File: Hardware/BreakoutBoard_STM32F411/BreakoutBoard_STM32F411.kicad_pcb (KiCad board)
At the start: 4 copper layers, 21.4 x 50.2 mm, 42 parts, among them IC101 STM32F411CCU6TR, IC401 TLV77333PDBVR, IC402 TLV77333PDBVR, J201 GSB1C41110SSHR, J202 PortB1, J203 PortB2, J204 PortA1, J205 PortA2, J403 Conn_02x03_Odd_Even, J404 SYS_JTAG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

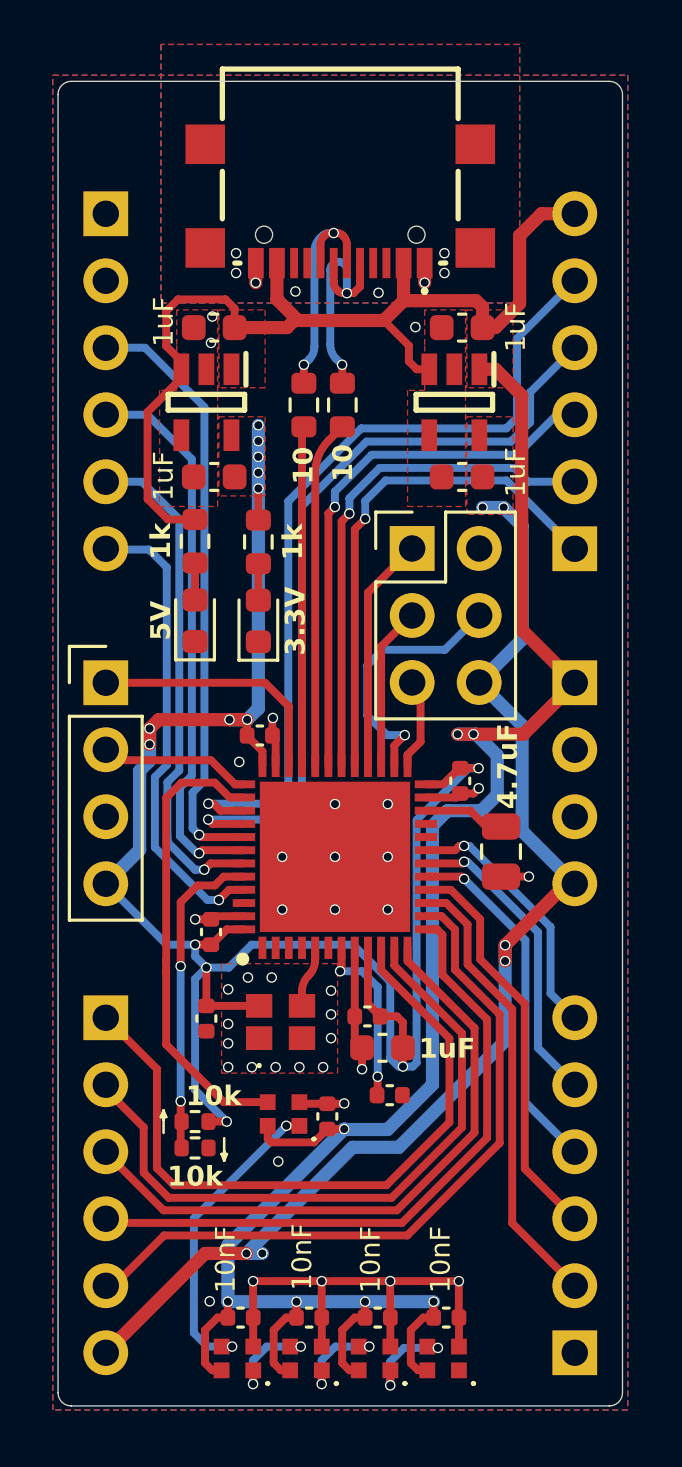
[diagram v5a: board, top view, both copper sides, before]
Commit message: added:labeling, changed:5V to 3V3P
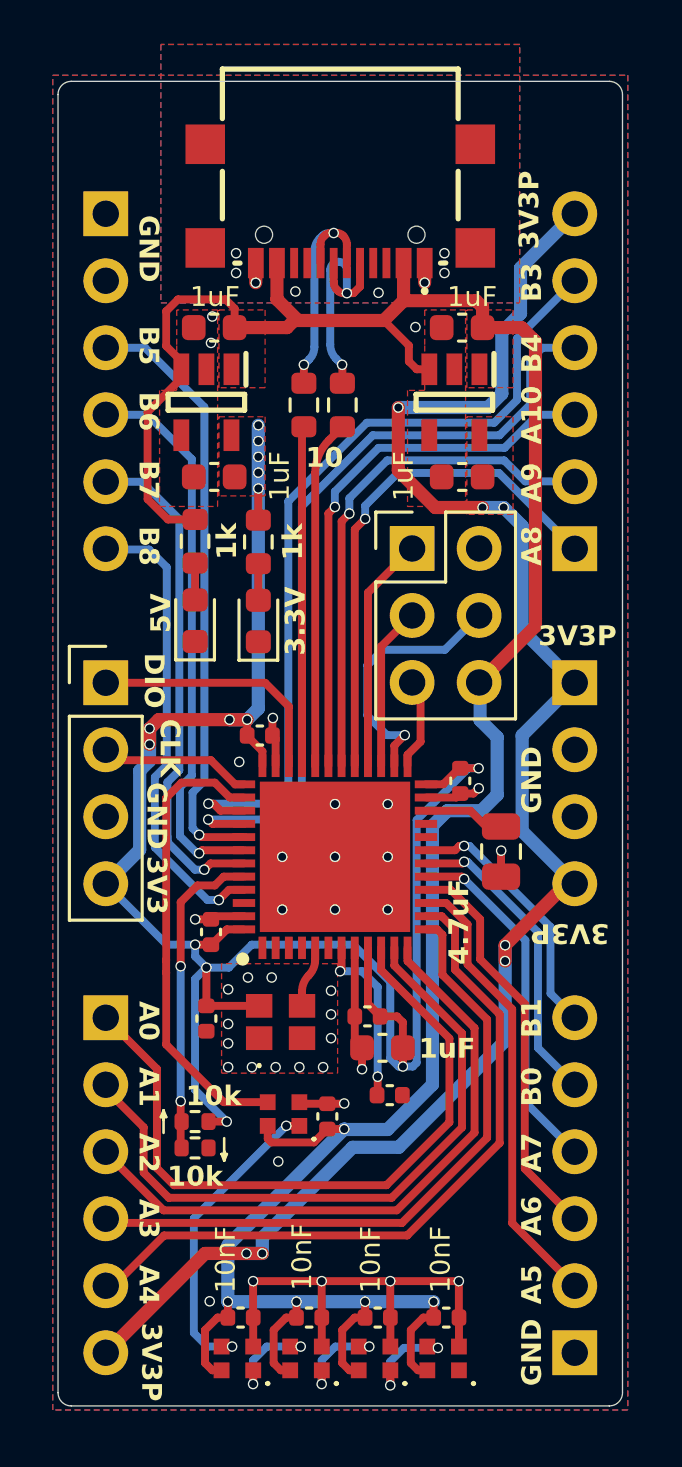
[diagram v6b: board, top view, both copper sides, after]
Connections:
- J204 pad 6: +5V -> +3.3VP
- J403 pad 6: +3.3VP -> +5V
- J405 pad 1: +5V -> +3.3VP
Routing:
- net +3.3VP: track 45.7 -> 65.3 mm, vias 6 -> 7
- net +5V: track 110.8 -> 102.3 mm, vias 7 -> 5
- net PA10: track 20.1 -> 20.8 mm
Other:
- board text added: "3V3"
- board text added: "3V3P"
- board text added: "A0"
- board text added: "A1"
- board text added: "A10"
- board text added: "A2"
- board text added: "A3"
- board text added: "A4"
- board text added: "A5"
- board text added: "A6"
- board text added: "A7"
- board text added: "A8"
- board text added: "A9"
- board text added: "B0"
- board text added: "B1"
- board text added: "B3"
- board text added: "B4"
- board text added: "B5"
- board text added: "B6"
- board text added: "B7"
- board text added: "B8"
- board text added: "CLK"
- board text added: "DIO"
- board text added: "GND"

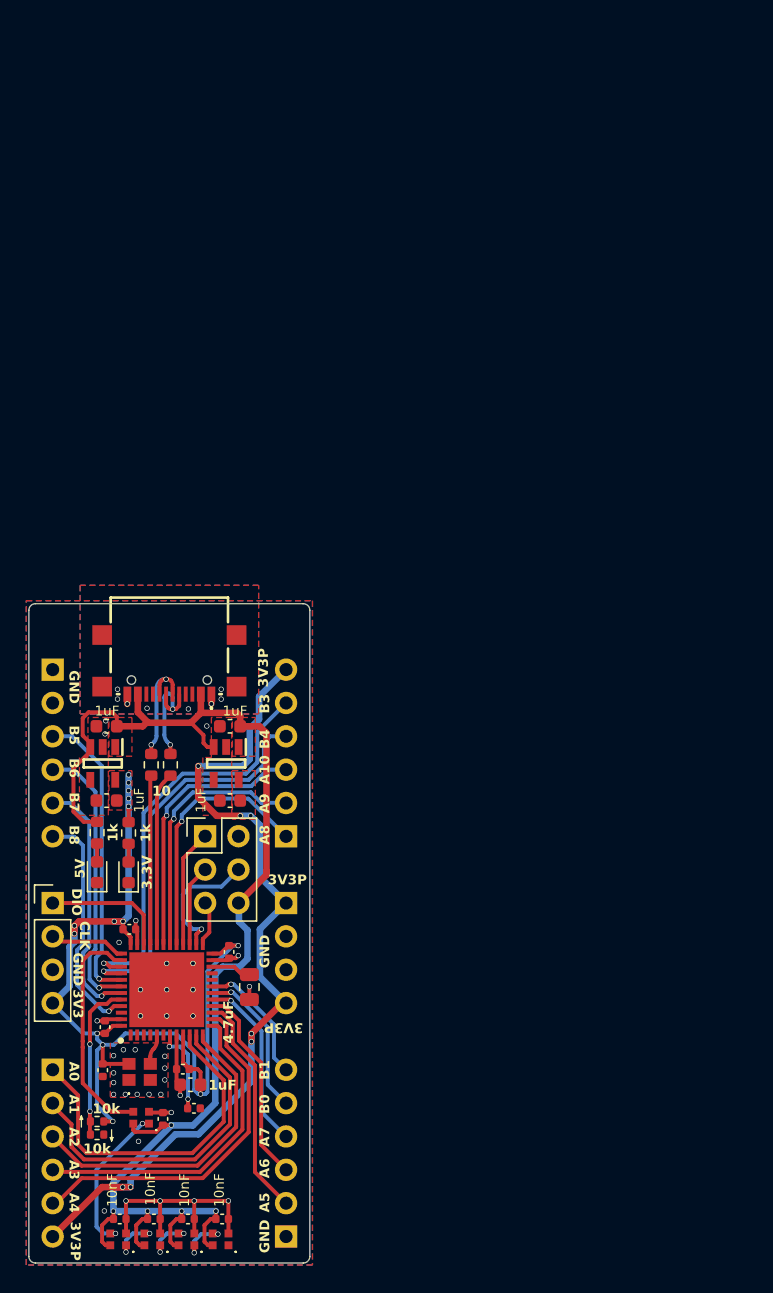
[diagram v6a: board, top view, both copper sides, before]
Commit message: fixed:edgecut, checked:pinheader spacing
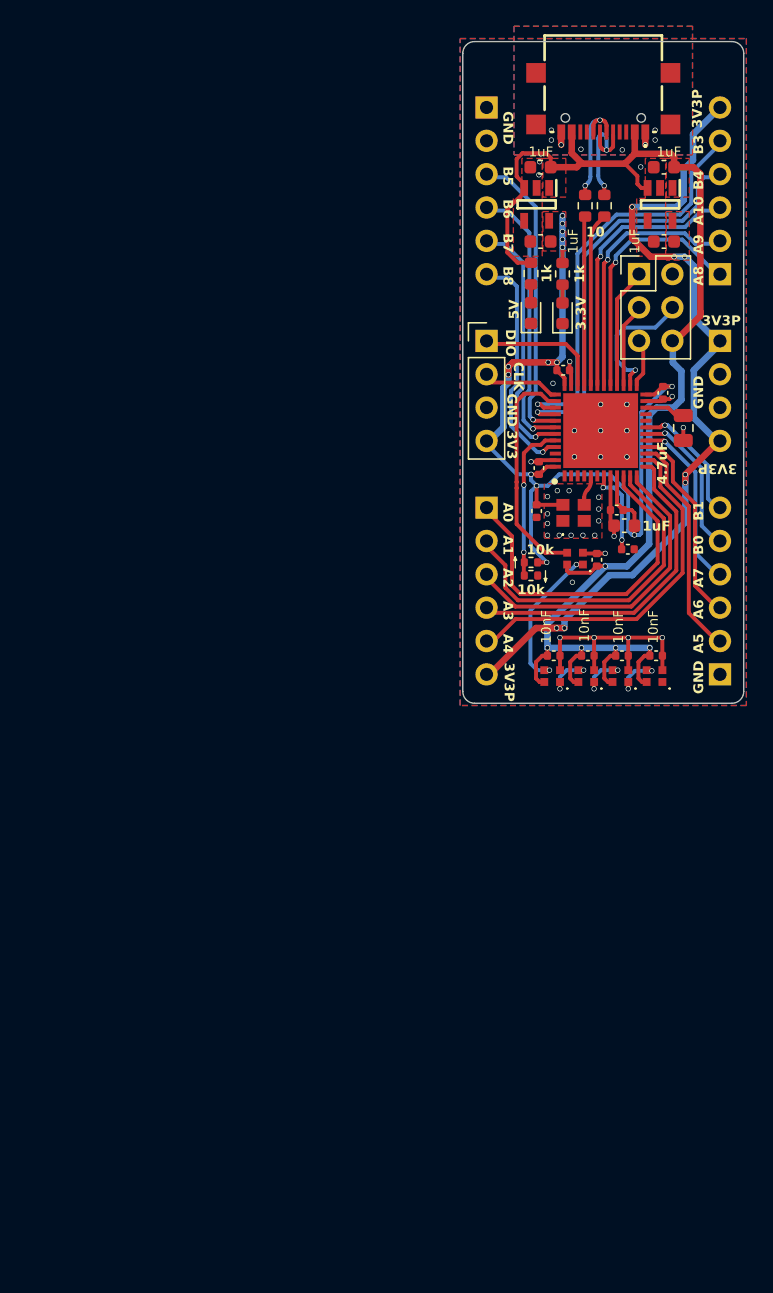
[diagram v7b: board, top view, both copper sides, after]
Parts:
- moved LED601 54.2 mm to (190.6, 108.6)
- moved LED701 54.2 mm to (193.2, 108.6)
- moved LED801 54.2 mm to (195.8, 108.6)
- moved C601 54.2 mm to (190.7, 107.1)
- moved C701 54.2 mm to (193.3, 107.1)
- moved C801 54.2 mm to (195.9, 107.1)
- moved C901 54.2 mm to (198.5, 107.1)
- moved LED901 54.2 mm to (198.4, 108.6)
- moved J203 54.1 mm to (203.3, 108.5)
- moved J204 54.1 mm to (203.3, 78.0)
- moved J205 54.1 mm to (185.6, 65.3)
- moved J403 54.1 mm to (197.2, 78.0)
- moved J404 54.1 mm to (185.6, 83.1)
- moved J405 54.1 mm to (203.3, 83.1)
- moved J201 54.1 mm to (194.4, 63.8)
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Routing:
- net GND: vias 45 -> 44
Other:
- board size 21.4 x 50.2 mm -> 21.4 x 50.4 mm

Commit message: ordering Version
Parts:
- C103: value 100nF -> 10nF
- moved J403 0.23 mm to (197.2, 78.3)
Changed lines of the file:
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@@
 		(attr through_hole)
 		(fp_line
-			(start 4.47 3.965)
-			(end 4.47 2.088)
-			(stroke
-				(width 0.2)
-				(type solid)
-			)
-			(layer "F.SilkS")
-		)
-		(fp_line
 			(start 4.47 0.088)
 			(end 4.47 -1.712)
@@
 		)
 		(fp_line
-			(start -4.47 3.965)
-			(end 4.47 3.965)
-			(stroke
-				(width 0.2)
-				(type solid)
-			)
-			(layer "F.SilkS")
-		)
-		(fp_line
-			(start -4.47 2.088)
-			(end -4.47 3.965)
-			(stroke
-				(width 0.2)
-				(type solid)
-			)
-			(layer "F.SilkS")
-		)
-		(fp_line
 			(start -4.47 -1.712)
 			(end -4.47 0.088)
@@
 	(footprint "Connector_PinHeader_2.54mm:PinHeader_2x03_P2.54mm_Vertical"
 		(layer "F.Cu")
-		(at 197.175 78.026)
+		(at 197.175 78.26)
 		(descr "Through hole straight pin header, 2x03, 2.54mm pitch, double rows")
 		(tags "Through hole pin header THT 2x03 2.54mm double row")
@@
 			)
 		)
-		(property "Value" "100nF"
-			(at 0 -1 90)
+		(property "Value" "10nF"
+			(at 0 -0.874 90)
 			(layer "F.SilkS")
-			(hide yes)
 			(effects
 				(font
@@
 	)
 	(gr_text "3V3P"
-		(at 186.85 107.616 270)
+		(at 186.8 107.2 270)
 		(layer "F.SilkS")
 		(effects
@@
 	)
 	(segment
-		(start 188.4 100.951)
-		(end 188.435 100.986)
-		(width 0.3)
-		(layer "F.Cu")
-		(net 6)
-	)
-	(segment
 		(start 189.695 91.035)
 		(end 190.03 90.7)
@@
 	(segment
 		(start 201.85 70.416)
-		(end 201.85 80.916)
+		(end 201.85 81.205)
 		(width 0.5)
 		(layer "F.Cu")
@@
 	(segment
 		(start 201.32 69.886)
-		(end 201.75 70.316)
+		(end 201.85 70.416)
 		(width 0.5)
 		(layer "F.Cu")
@@
 	)
 	(segment
-		(start 201.75 70.316)
-		(end 201.85 70.416)
-		(width 0.5)
-		(layer "F.Cu")
-		(net 12)
-	)
-	(segment
-		(start 201.85 80.916)
-		(end 201.85 81.205)
-		(width 0.5)
-		(layer "F.Cu")
-		(net 12)
-	)
-	(segment
 		(start 192.05 67.44)
 		(end 192.05 68.816)
@@
 	)
 	(segment
-		(start 199.75 83.375)
-		(end 199.715 83.34)
-		(width 0.5)
-		(layer "B.Cu")
-		(net 12)
-	)
-	(segment
 		(start 194.616 100.286)
 		(end 196.245 100.286)
@@
 	)
 	(segment
-		(start 193.7 66.726776)
-		(end 193.7 67.44)
-		(width 0.3)
-		(layer "F.Cu")
-		(net 16)
-	)
-	(segment
-		(start 194.538388 66.388388)
-		(end 194.575 66.425)
-		(width 0.3)
-		(layer "F.Cu")
-		(net 16)
-	)
-	(segment
-		(start 194.7 66.726776)
-		(end 194.7 67.44)
+		(start 193.7 66.490927)
+		(end 193.7 67.206)
 		(width 0.3)
 		(layer "F.Cu")
@@
 	)
 	(segment
-		(start 194.2 66.3)
-		(end 194.325 66.3)
+		(start 194.7 66.441421)
+		(end 194.7 67.206)
 		(width 0.3)
 		(layer "F.Cu")
@@
 	)
 	(segment
-		(start 193.861611 66.388388)
-		(end 193.825 66.425)
+		(start 193.833187 66.195812)
+		(end 193.8145 66.2145)
 		(width 0.3)
 		(layer "F.Cu")
@@
 	)
 	(segment
-		(start 194.075 66.3)
-		(end 194.2 66.3)
+		(start 194.0645 66.1)
+		(end 194.358578 66.1)
 		(width 0.3)
 		(layer "F.Cu")
@@
 	)
 	(via
-		(at 194.2 66.3)
+		(at 194.2 66.1)
 		(size 0.4)
 		(drill 0.3)
@@
 	)
 	(arc
-		(start 194.075 66.3)
-		(mid 193.959514 66.322971)
-		(end 193.861611 66.388388)
+		(start 193.8145 66.2145)
+		(mid 193.729757 66.341325)
+		(end 193.7 66.490927)
 		(width 0.3)
 		(layer "F.Cu")
@@
 	)
 	(arc
-		(start 194.575 66.425)
-		(mid 194.667513 66.563456)
-		(end 194.7 66.726776)
+		(start 194.0645 66.1)
+		(mid 193.939314 66.1249)
+		(end 193.833187 66.195812)
 		(width 0.3)
 		(layer "F.Cu")
@@
 	)
 	(arc
-		(start 194.538388 66.388388)
-		(mid 194.440484 66.322971)
-		(end 194.325 66.3)
+		(start 194.6 66.2)
+		(mid 194.67401 66.310764)
+		(end 194.7 66.441421)
 		(width 0.3)
 		(layer "F.Cu")
@@
 	)
 	(arc
-		(start 193.825 66.425)
-		(mid 193.732486 66.563456)
-		(end 193.7 66.726776)
+		(start 194.6 66.2)
+		(mid 194.489234 66.125989)
+		(end 194.358578 66.1)
 		(width 0.3)
 		(layer "F.Cu")
@@
 	)
 	(segment
-		(start 194.2 66.3)
-		(end 194.0375 66.3)
-		(width 0.3)
-		(layer "B.Cu")
-		(net 16)
-	)
-	(segment
-		(start 193.27 71.095)
-		(end 193.07 71.295)
+		(start 193.47 67.346187)
+		(end 193.47 70.612157)
 		(width 0.3)
 		(layer "B.Cu")
@@
 	)
 	(segment
-		(start 193.672499 66.502499)
-		(end 193.760095 66.414904)
+		(start 193.07 71.295)
+		(end 193.27 71.095)
 		(width 0.3)
 		(layer "B.Cu")
@@
 	)
 	(segment
-		(start 193.47 70.612157)
-		(end 193.47 66.991378)
+		(start 193.835 66.465)
+		(end 194.2 66.1)
 		(width 0.3)
 		(layer "B.Cu")
@@
 	)
 	(arc
-		(start 193.47 70.612157)
+		(start 193.27 71.095)
 		(mid 193.418021 70.873469)
-		(end 193.27 71.095)
-		(width 0.3)
-		(layer "B.Cu")
-		(net 16)
-	)
-	(arc
-		(start 194.0375 66.3)
-		(mid 193.887369 66.329862)
-		(end 193.760095 66.414904)
+		(end 193.47 70.612157)
 		(width 0.3)
 		(layer "B.Cu")
@@
 	)
 	(arc
-		(start 193.672499 66.502499)
-		(mid 193.522627 66.726798)
-		(end 193.47 66.991378)
+		(start 193.835 66.465)
+		(mid 193.56486 66.869292)
+		(end 193.47 67.346187)
 		(width 0.3)
 		(layer "B.Cu")
@@
 	)
 	(segment
-		(start 194.919 100.962)
-		(end 192.2575 103.6235)
-		(width 0.5)
-		(layer "B.Cu")
-		(net 27)
-	)
-	(segment
 		(start 200.645 76.706)
 		(end 201.345 77.406)
@@
 	)
 	(segment
-		(start 192.2575 103.6235)
-		(end 191.495003 104.385997)
+		(start 191.495003 104.385997)
+		(end 194.919 100.962)
 		(width 0.5)
 		(layer "B.Cu")
@@
 	)
 	(segment
-		(start 187.897 89.392232)
-		(end 187.897 89.166)
-		(width 0.3)
-		(layer "B.Cu")
-		(net 30)
-	)
-	(segment
 		(start 186.93 75.73)
 		(end 185.56 75.73)
@@
 	)
 	(segment
-		(start 203.326 75.716)
-		(end 203.34 75.73)
-		(width 0.3)
-		(layer "B.Cu")
-		(net 31)
-	)
-	(segment
 		(start 194.795 76.936)
 		(end 194.795 76.355)
@@
 			"9061a6f7-eedd-483a-aec2-3530d2bac3f8" "90b166ae-a0ea-4d6e-8b0b-4fde08300241"
 			"936b8314-0eb6-4224-8117-2000cd565a02" "97bbe1d8-72db-4914-9a70-fd7c72119746"
-			"984f31a5-17ad-4061-8313-116940e000dd" "991fb4ac-1f2a-4d77-8cf2-79be67d57af3"
-			"9cb01bc6-f38f-4fba-b2ba-33f76ca87221" "9cd24a0e-a724-4348-b8ad-484d0c1a3001"
-			"9d644d6d-1e8b-423e-a5e4-a25d8ca834ef" "9d738cbf-352f-40ce-b5aa-fa63ccd88a1a"
-			"9e18b3f2-1e46-49a2-a706-e4cac73ffcb8" "a1d5b478-9ac3-4b28-8aae-2988abdd0572"
-			"a351a675-6d8b-4ff2-8748-2cb112c3b405" "a53f6680-eaba-4985-ac9e-ed84e3df646a"
-			"a555c708-b102-4f1a-be2a-a689c23cd8ec" "ab333ac0-a337-41c5-9150-578df3b367e6"
-			"b1eab8bd-b6ba-492d-aac5-a8e8896055d8" "b2217b2a-8e00-4a06-b598-266261e4eca8"
-			"b26543e5-96d5-4b91-8413-00303e6b4274" "b3a3bb48-13a9-400a-a722-dbda411d75c0"
-			"b458ac56-e53f-4d13-84c4-92fb74e09e12" "b4da50cf-0282-4bf5-923d-be5a7b8191e0"
-			"b602e55f-b784-4f36-a5f3-84856b895711" "bfcf2464-90be-4c06-9f70-c4a3a912ad30"
-			"bfebfd38-61cd-4705-960c-bdce302ebfb5" "c57a648f-f596-4ca3-b35d-0cd6752680e2"
-			"c664858a-f964-497c-8b71-8a1ccb30c498" "c72a436c-2bdd-42ce-91d9-954576c4727f"
-			"c8b13321-2ba2-41bf-a993-9f90bcd615a5" "c8f8d109-0595-41b5-bcce-7cb4bd7cf8e0"
-			"cac0fa3d-05a8-4515-90c7-5fe0d7916d1d" "cd0c786f-1a32-4fc4-8c24-38417479ae6b"
-			"d0a241f3-d2bd-4745-8e01-00debd98c49c" "d143fa5b-8cab-4841-9d66-2129df6020aa"
-			"d763e94b-b635-4bec-9953-ca6525b68e35" "dac34644-a048-4e1b-b88a-4f5232ee763c"
-			"dc3b8b37-aac5-49f6-b07b-07e300ca9e31" "dfb37506-ca03-4e47-8074-ac52613f0644"
-			"dfec2621-b790-4109-92d0-f6b09e22c382" "e12d0c51-8cfb-4a45-9466-9ca911815a68"
-			"e304ad46-f9f9-42dc-bc7b-086198585db6" "e42ec4d1-e99e-44af-b534-4d5318db9cfa"
-			"e4bfd52b-f2a3-42d7-8cdf-fcb16f10c8f5" "e554f08f-1b4f-4c6f-82fa-140e659def1f"
-			"e5761d27-32e3-4733-b706-b9df3f760663" "e7dbbc27-b770-434d-b0ba-3e0cd8fb83c5"
-			"ea481244-7b68-44be-9d90-44ff0322417b" "ec2de171-9bc3-40fb-83bd-fa82f9cdc5f6"
-			"ec93b996-df20-4e16-94bc-281965e20196" "ee8a0531-57a4-41d8-8d52-f9ba57b33260"
-			"f310699c-b07c-4404-81c6-a341fc22b8b7" "f9fdce73-7e40-4588-8f04-669e471fcb59"
-			"fa182eb2-8ef1-4d65-95db-af8f546a3777" "fb4dcbba-132f-442f-8eb4-98ca91fb56aa"
+			"984f31a5-17ad-4061-8313-116940e000dd" "9cb01bc6-f38f-4fba-b2ba-33f76ca87221"
+			"9cd24a0e-a724-4348-b8ad-484d0c1a3001" "9d644d6d-1e8b-423e-a5e4-a25d8ca834ef"
+			"9d738cbf-352f-40ce-b5aa-fa63ccd88a1a" "9e18b3f2-1e46-49a2-a706-e4cac73ffcb8"
+			"a1d5b478-9ac3-4b28-8aae-2988abdd0572" "a351a675-6d8b-4ff2-8748-2cb112c3b405"
+			"a53f6680-eaba-4985-ac9e-ed84e3df646a" "a555c708-b102-4f1a-be2a-a689c23cd8ec"
+			"ab333ac0-a337-41c5-9150-578df3b367e6" "b1eab8bd-b6ba-492d-aac5-a8e8896055d8"
+			"b2217b2a-8e00-4a06-b598-266261e4eca8" "b26543e5-96d5-4b91-8413-00303e6b4274"
+			"b3a3bb48-13a9-400a-a722-dbda411d75c0" "b458ac56-e53f-4d13-84c4-92fb74e09e12"
+			"b4da50cf-0282-4bf5-923d-be5a7b8191e0" "b602e55f-b784-4f36-a5f3-84856b895711"
+			"bfcf2464-90be-4c06-9f70-c4a3a912ad30" "bfebfd38-61cd-4705-960c-bdce302ebfb5"
+			"c57a648f-f596-4ca3-b35d-0cd6752680e2" "c664858a-f964-497c-8b71-8a1ccb30c498"
+			"c72a436c-2bdd-42ce-91d9-954576c4727f" "c8b13321-2ba2-41bf-a993-9f90bcd615a5"
+			"c8f8d109-0595-41b5-bcce-7cb4bd7cf8e0" "cac0fa3d-05a8-4515-90c7-5fe0d7916d1d"
+			"cd0c786f-1a32-4fc4-8c24-38417479ae6b" "d0a241f3-d2bd-4745-8e01-00debd98c49c"
+			"d143fa5b-8cab-4841-9d66-2129df6020aa" "d763e94b-b635-4bec-9953-ca6525b68e35"
+			"dac34644-a048-4e1b-b88a-4f5232ee763c" "dc3b8b37-aac5-49f6-b07b-07e300ca9e31"
+			"dfb37506-ca03-4e47-8074-ac52613f0644" "dfec2621-b790-4109-92d0-f6b09e22c382"
+			"e12d0c51-8cfb-4a45-9466-9ca911815a68" "e304ad46-f9f9-42dc-bc7b-086198585db6"
+			"e42ec4d1-e99e-44af-b534-4d5318db9cfa" "e4bfd52b-f2a3-42d7-8cdf-fcb16f10c8f5"
+			"e554f08f-1b4f-4c6f-82fa-140e659def1f" "e5761d27-32e3-4733-b706-b9df3f760663"
+			"e7dbbc27-b770-434d-b0ba-3e0cd8fb83c5" "ea481244-7b68-44be-9d90-44ff0322417b"
+			"ec2de171-9bc3-40fb-83bd-fa82f9cdc5f6" "ec93b996-df20-4e16-94bc-281965e20196"
+			"ee8a0531-57a4-41d8-8d52-f9ba57b33260" "f310699c-b07c-4404-81c6-a341fc22b8b7"
+			"f9fdce73-7e40-4588-8f04-669e471fcb59" "fa182eb2-8ef1-4d65-95db-af8f546a3777"
+			"fb4dcbba-132f-442f-8eb4-98ca91fb56aa"
 		)
 	)
